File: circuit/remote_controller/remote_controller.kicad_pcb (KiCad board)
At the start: 2 copper layers, 39.6 x 101 mm, 68 parts, among them J1 Conn_01x02_Male, J2 USB_C_Receptacle_USB2.0, Q1 SS8050-G, Q2 SS8050-G, U1 LT1963AxST-3.3, U2 ESP32-WROVER-B, U3 CP2102N-Axx-xQFN28

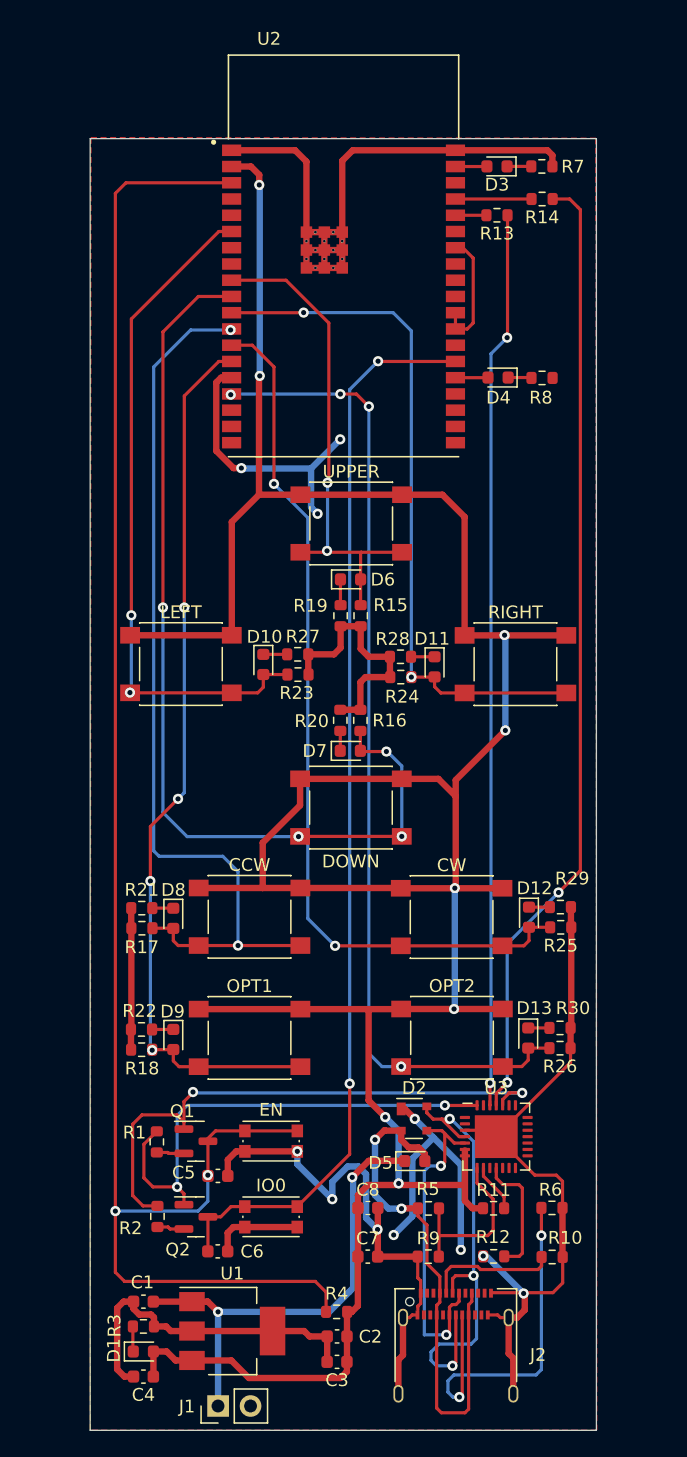
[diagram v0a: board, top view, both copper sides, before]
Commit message: Apply the circuit design; add holes at each corner.
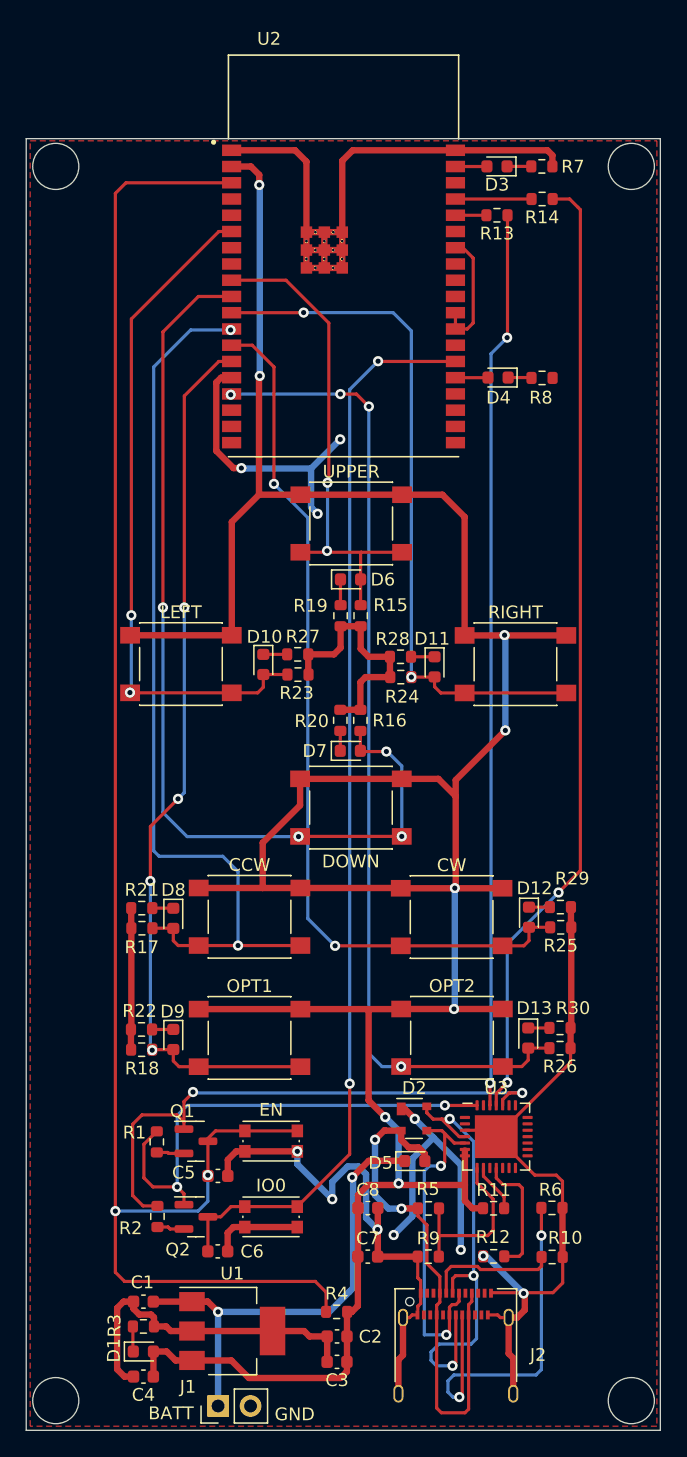
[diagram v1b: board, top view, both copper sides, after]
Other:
- board size 39.6 x 101 mm -> 49.6 x 101 mm
- board text added: "BATT"
- board text added: "GND"
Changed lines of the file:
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@@
     )
     (pad_to_mask_clearance 0)
+    (aux_axis_origin 80 130)
     (pcbplotparams
       (layerselection 0x00010fc_ffffffff)
       (disableapertmacros false)
-      (usegerberextensions false)
+      (usegerberextensions true)
       (usegerberattributes true)
       (usegerberadvancedattributes true)
@@
       (outputformat 1)
       (mirror false)
-      (drillshape 1)
+      (drillshape 0)
       (scaleselection 1)
-      (outputdirectory "")
+      (outputdirectory "plot/")
     )
   )
@@
     (property "Sheetname" "")
     (attr through_hole)
-    (fp_text reference "J1" (at -0.04 -2.43 180) (layer "F.SilkS")
+    (fp_text reference "J1" (at 1.5 -2.36 180) (layer "F.SilkS")
       (effects (font (size 1 1) (thickness 0.15)))
     )
@@
     )
   )
-  (gr_rect (start 85.19 28.83) (end 124.77 129.82) (layer "Edge.Cuts") (width 0.1) (fill none))
+  (gr_circle (center 127.5 31) (end 128.5 29.5) (layer "Edge.Cuts") (width 0.1) (fill none))
+  (gr_rect (start 80.19 28.83) (end 129.77 129.82) (layer "Edge.Cuts") (width 0.1) (fill none))
+  (gr_circle (center 82.5 127.5) (end 81 128.5) (layer "Edge.Cuts") (width 0.1) (fill none))
+  (gr_circle (center 127.5 127.5) (end 129 128.5) (layer "Edge.Cuts") (width 0.1) (fill none))
+  (gr_circle (center 82.5 31) (end 84 32) (layer "Edge.Cuts") (width 0.1) (fill none))
+  (gr_text "GND" (at 101.18 128.57) (layer "F.SilkS")
+    (effects (font (size 1 1) (thickness 0.15)))
+  )
+  (gr_text "BATT" (at 91.51 128.49) (layer "F.SilkS")
+    (effects (font (size 1 1) (thickness 0.15)))
+  )
   (segment (start 90.13 119.76) (end 93.15 119.76) (width 0.5) (layer "F.Cu") (net 1))
   (segment (start 106.97 108.75) (end 109.7625 108.75) (width 0.5) (layer "F.Cu") (net 1))
@@
     (polygon
       (pts
-        (xy 124.73 28.8)
-        (xy 124.8 129.79)
-        (xy 85.2 129.81)
-        (xy 85.25 28.75)
+        (xy 129.5 129.5)
+        (xy 80.5 129.5)
+        (xy 80.5 29)
+        (xy 129.5 29)
       )
     )
